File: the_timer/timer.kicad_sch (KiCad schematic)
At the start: 20 parts, among them J1 AVR-ISP-6, J2 Conn_01x04_Socket, J3 Conn_01x02_Socket, Q1 2N7002, Q2 2N7002, Q3 2N7002, U1 ATtiny48-A, U2 TPS61033, U3 MC3416, U4 W25Q128JVS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

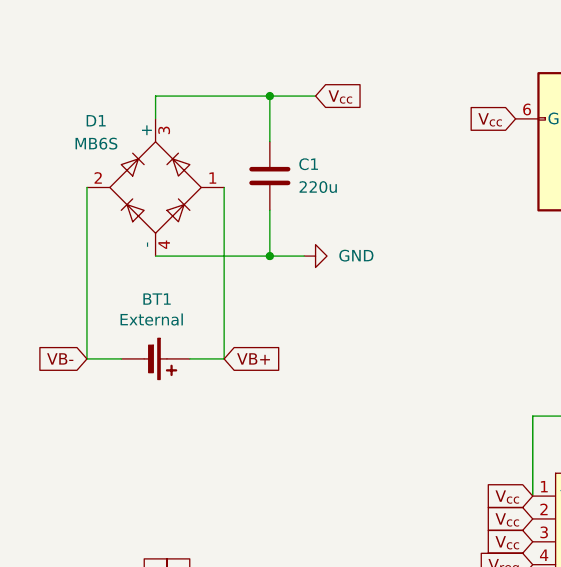
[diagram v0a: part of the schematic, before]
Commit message: repair timer files from the merge
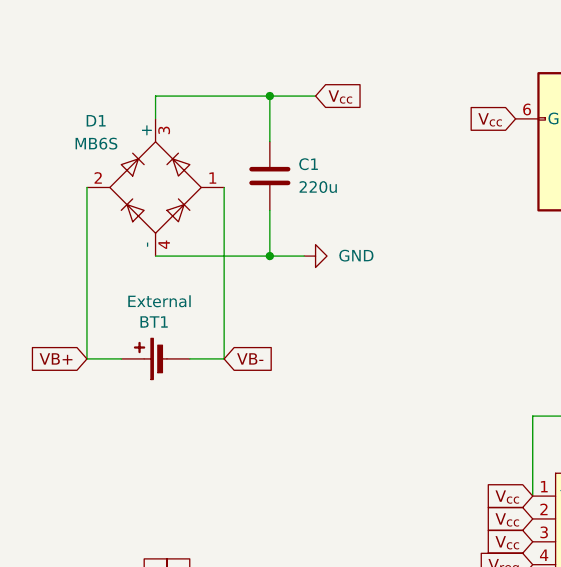
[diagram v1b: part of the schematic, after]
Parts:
- BT1: footprint locals:CONN2_1775469-2_TEC -> locals:TE Right Angle JST
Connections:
- net VB+: now also D1.2; no longer D1.1
- net VB-: now also D1.1; no longer D1.2
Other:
- moved on the sheet: BT1

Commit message: weekends'
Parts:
- C1: DKPN (none) -> STOCK
- D1: DKPN (none) -> MB6SCT-ND
- H1, H2, H3, J1, J2, J3: DKPN (none) -> CONN
- U4: DKPN (none) -> W25Q128JVSIQ-ND
- U5: DKPN (none) -> 223-1198-1-ND
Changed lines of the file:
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@@
+			)
+		)
+		(property "DKPN" "CONN"
+			(at 85.725 33.02 0)
+			(effects
+				(font
+					(size 1.27 1.27)
+				)
+				(hide yes)
 			)
 		)
@@
 			)
 		)
+		(property "DKPN" "CONN"
+			(at 184.15 92.71 0)
+			(effects
+				(font
+					(size 1.27 1.27)
+				)
+				(hide yes)
+			)
+		)
 		(pin "1"
 		)
@@
 			)
 		)
+		(property "DKPN" "CONN"
+			(at 109.22 149.86 0)
+			(effects
+				(font
+					(size 1.27 1.27)
+				)
+				(hide yes)
+			)
+		)
 		(instances
 			(project "timer"
@@
 			)
 		)
+		(property "DKPN" "CONN"
+			(at 185.42 111.76 0)
+			(effects
+				(font
+					(size 1.27 1.27)
+				)
+				(hide yes)
+			)
+		)
 		(pin "1"
 		)
@@
 			)
 		)
-		(property "DKPN" ""
+		(property "DKPN" "STOCK"
 			(at 48.26 36.83 0)
 			(effects
@@
 			)
 		)
+		(property "DKPN" "W25Q128JVSIQ-ND"
+			(at 87.63 113.03 0)
+			(effects
+				(font
+					(size 1.27 1.27)
+				)
+				(hide yes)
+			)
+		)
 		(pin "6"
 		)
@@
 		)
 		(property "Description" "Miniature Glass Passivated Single-Phase Surface Mount Bridge Rectifiers, 700V Vrms, 1.0A If, DFS SMD package"
+			(at 35.56 38.1 0)
+			(effects
+				(font
+					(size 1.27 1.27)
+				)
+				(hide yes)
+			)
+		)
+		(property "DKPN" "MB6SCT-ND"
 			(at 35.56 38.1 0)
 			(effects
@@
 			)
 		)
+		(property "DKPN" "CONN"
+			(at 82.55 149.86 0)
+			(effects
+				(font
+					(size 1.27 1.27)
+				)
+				(hide yes)
+			)
+		)
 		(instances
 			(project "timer"
@@
 			)
 		)
+		(property "DKPN" "CONN"
+			(at 137.16 149.86 0)
+			(effects
+				(font
+					(size 1.27 1.27)
+				)
+				(hide yes)
+			)
+		)
 		(instances
 			(project "timer"
@@
 			(at 139.7 110.49 0)
 			(effects
+				(font
+					(size 1.27 1.27)
+				)
+				(hide yes)
+			)
+		)
+		(property "DKPN" "223-1198-1-ND"
+			(at 139.7 110.49 0)
+			(effects

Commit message: Added decoupling cap to barometer and rotated IMU 45 deg
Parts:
- added C2: 100n, Capacitor_SMD:C_0603_1608Metric, symbol Device:C_Small
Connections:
- net GND: now also C2.2
- net V_{reg}: now also C2.1
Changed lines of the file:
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@@
 	)
 	(junction
+		(at 139.7 120.65)
+		(diameter 0)
+		(color 0 0 0 0)
+	)
+	(junction
 		(at 107.95 72.39)
 		(diameter 0)
@@
 	(wire
 		(pts
+			(xy 153.67 120.65) (xy 153.67 113.03)
+		)
+		(stroke
+			(width 0)
+			(type default)
+		)
+	)
+	(wire
+		(pts
 			(xy 85.09 63.5) (xy 77.47 63.5)
 		)
@@
 	(wire
 		(pts
+			(xy 139.7 100.33) (xy 153.67 100.33)
+		)
+		(stroke
+			(width 0)
+			(type default)
+		)
+	)
+	(wire
+		(pts
 			(xy 39.37 57.15) (xy 43.18 57.15)
 		)
@@
 	(wire
 		(pts
+			(xy 153.67 100.33) (xy 153.67 107.95)
+		)
+		(stroke
+			(width 0)
+			(type default)
+		)
+	)
+	(wire
+		(pts
 			(xy 90.17 63.5) (xy 99.06 63.5)
 		)
@@
 	(wire
 		(pts
+			(xy 139.7 120.65) (xy 153.67 120.65)
+		)
+		(stroke
+			(width 0)
+			(type default)
+		)
+	)
+	(wire
+		(pts
 			(xy 31.75 57.15) (xy 27.94 57.15)
 		)
@@
 	)
 	(symbol
+		(lib_id "Device:C_Small")
+		(at 153.67 110.49 0)
+		(unit 1)
+		(exclude_from_sim no)
+		(in_bom yes)
+		(on_board yes)
+		(dnp no)
+		(fields_autoplaced yes)
+		(property "Reference" "C2"
+			(at 156.21 109.2262 0)
+			(effects
+				(font
+					(size 1.27 1.27)
+				)
+				(justify left)
+			)
+		)
+		(property "Value" "100n"
+			(at 156.21 111.7662 0)
+			(effects
+				(font
+					(size 1.27 1.27)
+				)
+				(justify left)
+			)
+		)
+		(property "Footprint" "Capacitor_SMD:C_0603_1608Metric"
+			(at 153.67 110.49 0)
+			(effects
+				(font
+					(size 1.27 1.27)
+				)
+				(hide yes)
+			)
+		)
+		(property "Datasheet" "~"
+			(at 153.67 110.49 0)
+			(effects
+				(font
+					(size 1.27 1.27)
+				)
+				(hide yes)
+			)
+		)
+		(property "Description" "Unpolarized capacitor, small symbol"
+			(at 153.67 110.49 0)
+			(effects
+				(font
+					(size 1.27 1.27)
+				)
+				(hide yes)
+			)
+		)
+		(pin "2"
+		)
+		(pin "1"
+		)
+		(instances
+			(project "timer"
+				(path "/e2b0a296-fcac-4dcc-93f1-26b3dc1147d1"
+					(reference "C2")
+					(unit 1)
+				)
+			)
+		)
+	)
+	(symbol
 		(lib_id "globals:MC3416")
 		(at 135.255 34.925 0)
@@
 		(on_board yes)
 		(dnp no)
-		(fields_autoplaced yes)
 		(property "Reference" "#PWR013"
 			(at 123.19 115.57 0)
@@
 		)
 		(property "Value" "GND"
-			(at 125.73 115.5699 90)
+			(at 129.794 118.11 90)
 			(effects
 				(font
@@
 		(on_board yes)
 		(dnp no)
-		(fields_autoplaced yes)
 		(property "Reference" "U5"
-			(at 148.59 109.2199 0)
+			(at 121.666 95.25 0)
 			(effects
 				(font
@@
 		)
 		(property "Value" "MS5607-02BA"
-			(at 148.59 111.7599 0)
+			(at 121.666 97.79 0)
 			(effects
 				(font

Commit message: Updated barometer decoupling cap DKPN
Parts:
- C2: DKPN (none) -> 3372-0603B104J500XDTR-ND
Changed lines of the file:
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@@
 		(title "Timer")
 		(date "2024-04-16")
-		(rev "0.0.2")
+		(rev "0.0.3")
 		(company "Mines Rocket Club")
 		(comment 1 "William Layne")
@@
 			(at 153.67 110.49 0)
 			(effects
+				(font
+					(size 1.27 1.27)
+				)
+				(hide yes)
+			)
+		)
+		(property "DKPN" "3372-0603B104J500XDTR-ND"
+			(at 153.67 110.49 0)
+			(effects

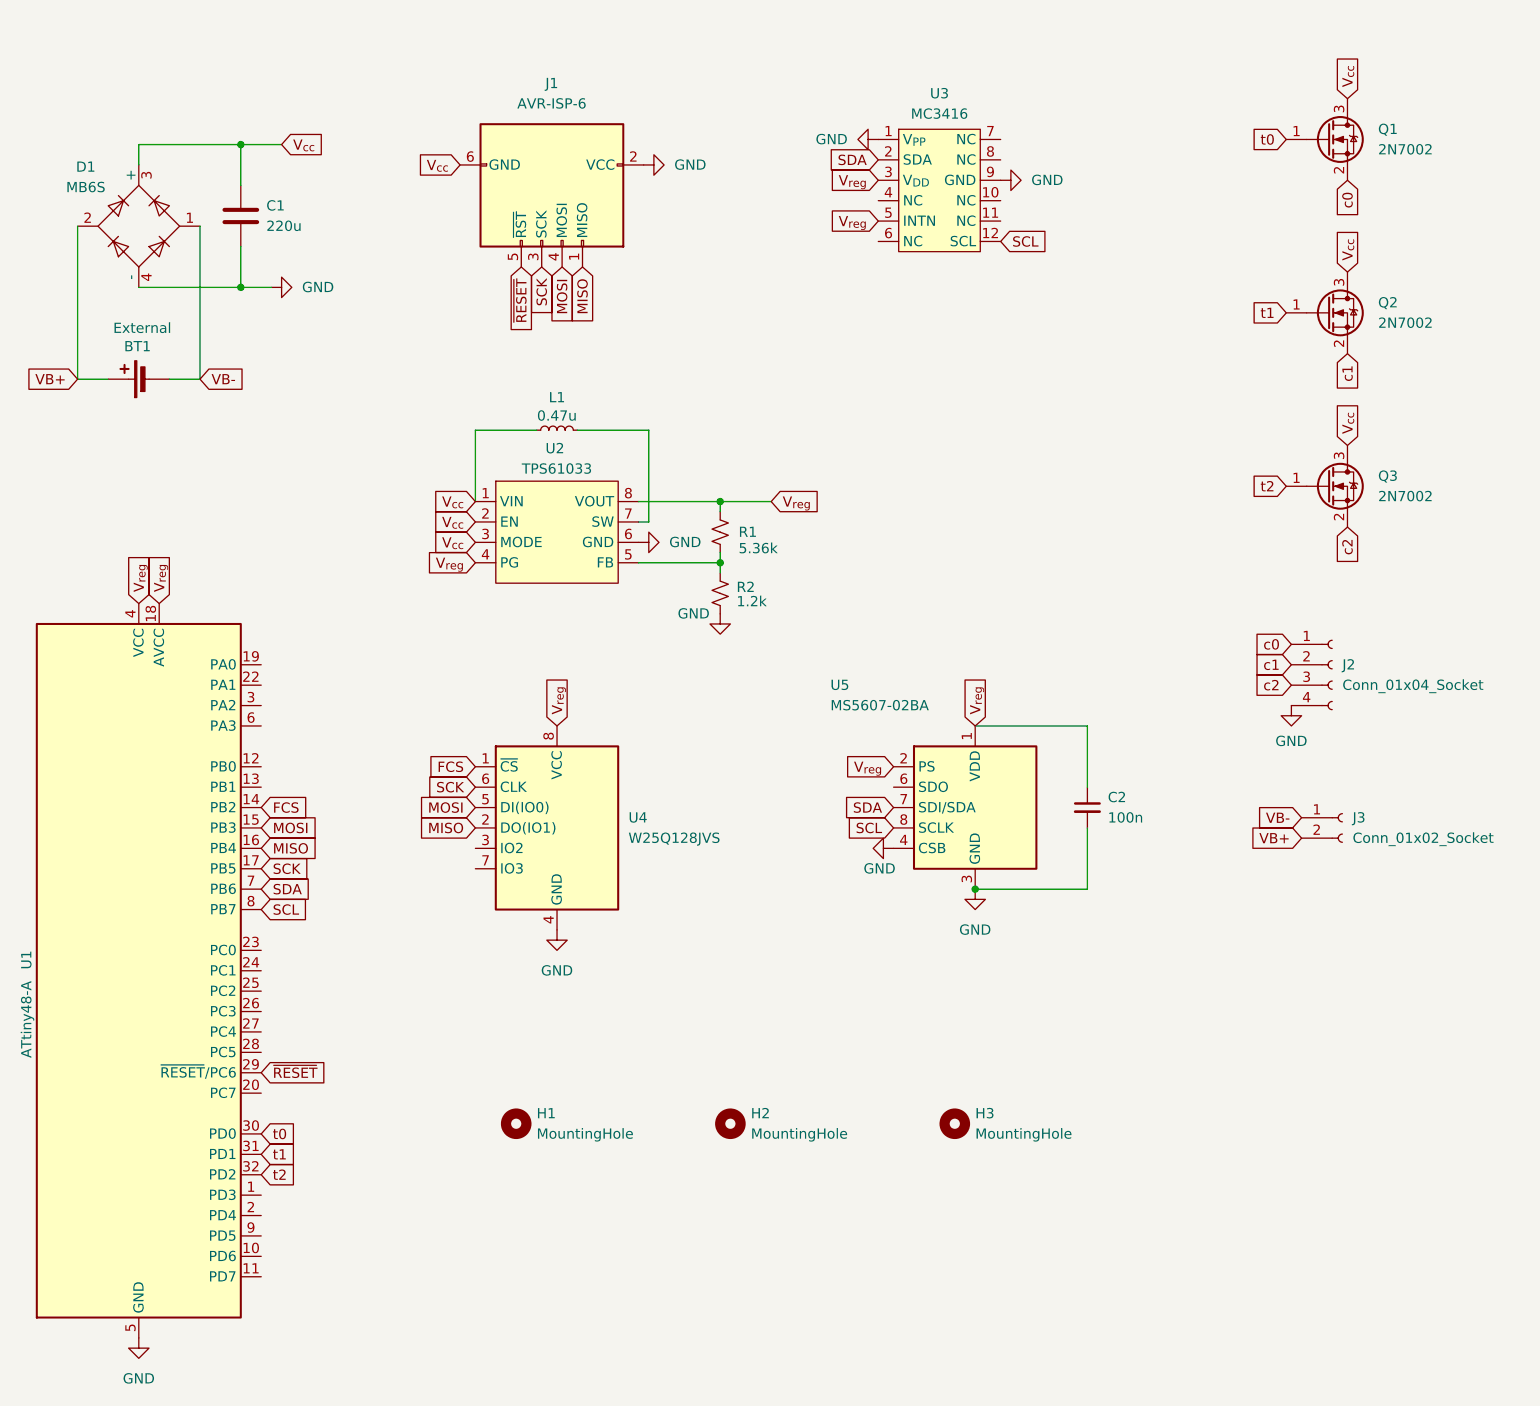
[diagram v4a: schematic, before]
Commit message: Standardized names on Timer schematic
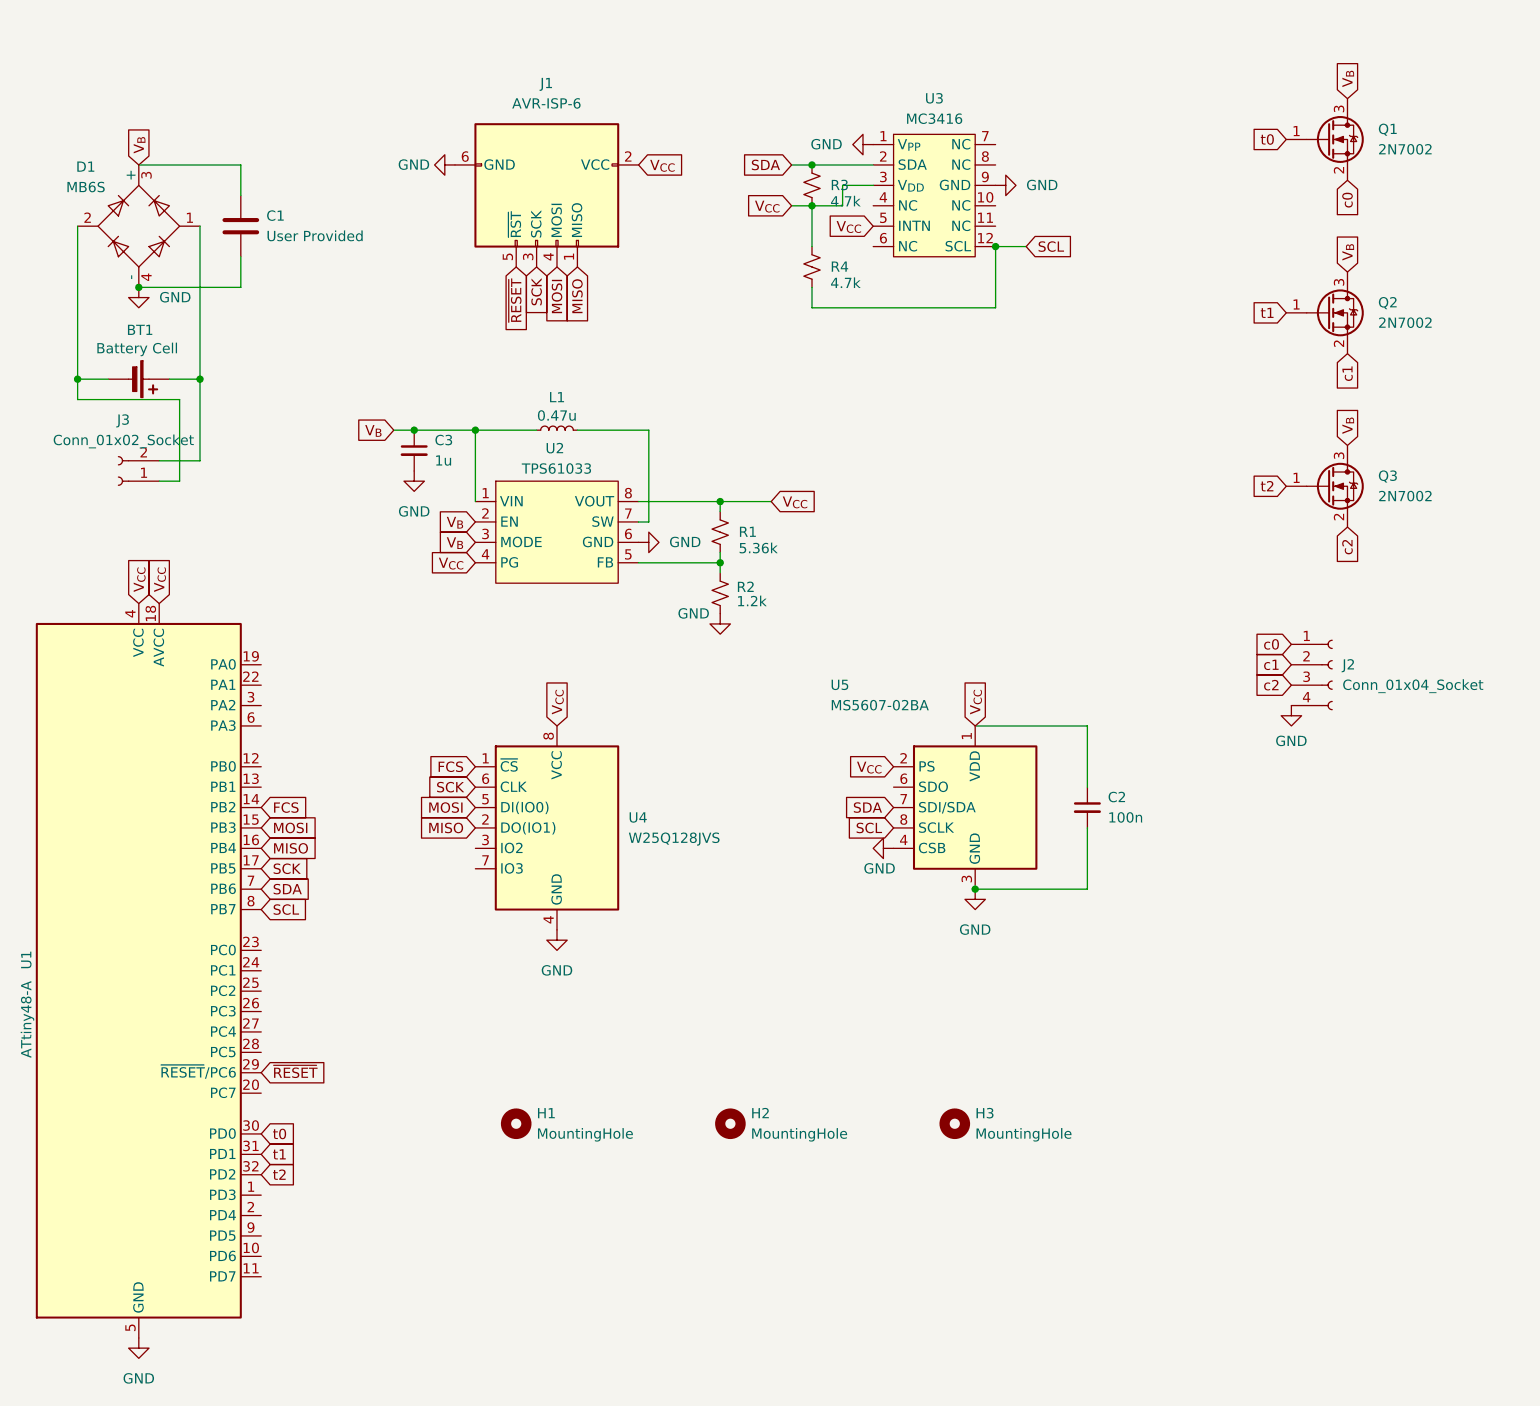
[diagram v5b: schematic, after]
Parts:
- added C3: 1u, Capacitor_SMD:C_0603_1608Metric, symbol Device:C_Small
- added R3, R4: 4.7k, Resistor_SMD:R_0603_1608Metric, symbol Device:R_Small_US
- BT1: value External -> Battery Cell; footprint locals:TE Right Angle JST -> locals_but_working_PLEASE:CONN2_1775469-2_TEC
- C1: value 220u -> User Provided; footprint Capacitor_THT:CP_Radial_D5.0mm_P2.00mm -> Connector_Wire:SolderWire-0.5sqmm_1x02_P4.8mm_D0.9mm_OD2.3mm; DKPN STOCK -> (none)
- C2: DKPN 3372-0603B104J500XDTR-ND -> 732-7989-1-ND
- L1: DKPN 490-LQM18DN470M70LCT-ND -> 732-7447860247CT-ND
- R1: DKPN RN73H1JTTD5361F10 -> RMCF0603FT5K36CT-ND
- R2: DKPN RN73R1JTTD1201F10 -> RMCF0603FT1K20CT-ND
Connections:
- net GND: now also J1.6 (GND), C3.2; no longer J1.2 (VCC)
- net SCL: now also R4.2
- net SDA: now also R3.1
- net VB+: no longer names the net of BT1.1 (+), J3.2 (Pin_2)
- net VB+: now also D1.1; no longer D1.2
- net VB-: no longer names the net of BT1.2 (-), J3.1 (Pin_1)
- net VB-: now also D1.2; no longer D1.1
- net V_{cc} renamed V_{B}
- net V_{B}: now also C3.1; no longer J1.6 (GND)
- net V_{reg} renamed V_{CC}
- net V_{CC}: now also J1.2 (VCC), R3.2, R4.1
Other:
- moved on the sheet: BT1, C1, J1, J3, U3

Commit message: gathered data on pyro charges
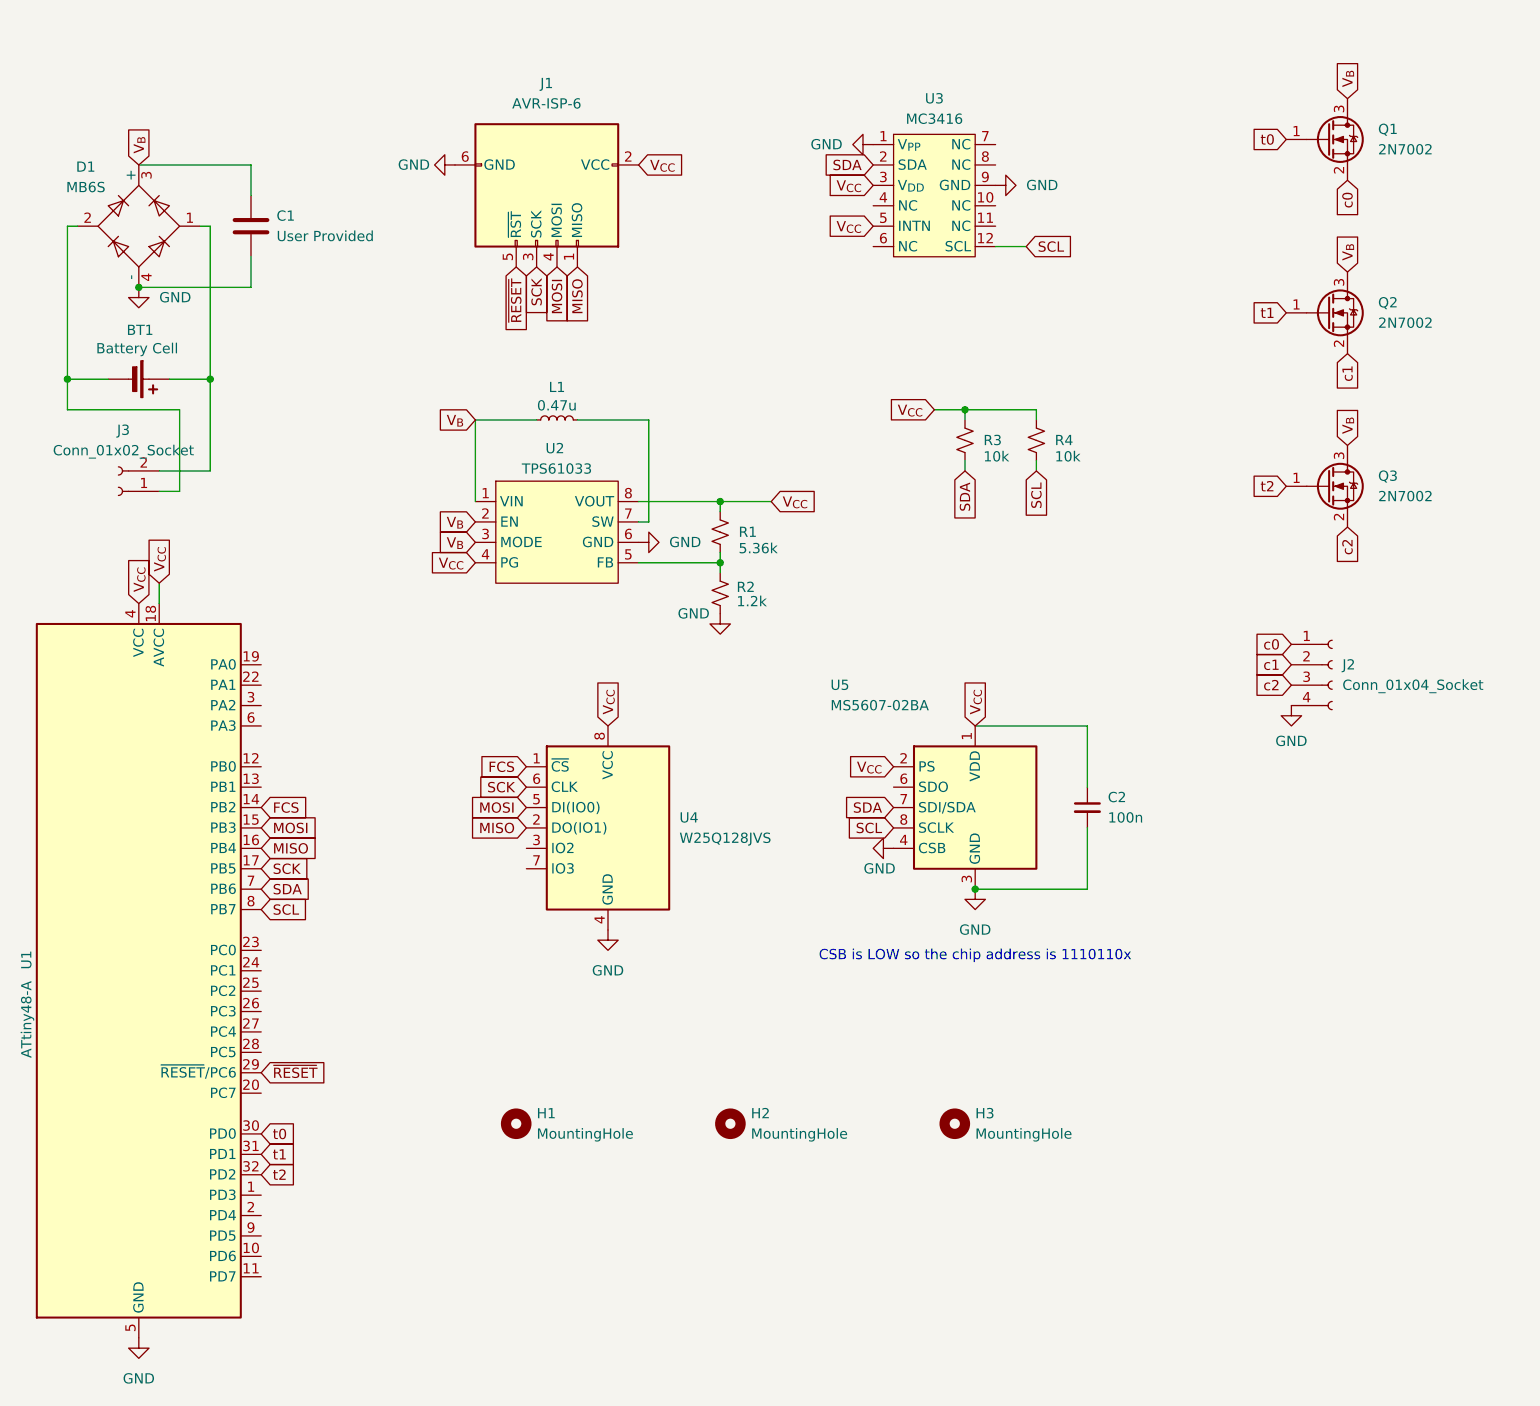
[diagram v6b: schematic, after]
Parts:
- removed C3: 1u, Capacitor_SMD:C_0603_1608Metric, symbol Device:C_Small
- R3, R4: value 4.7k -> 10k; DKPN RMCF0603FT4K70CT-ND -> RMCF0603JT10K0CT-ND
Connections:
- net SDA: now also R3.2; no longer R3.1
- net V_{CC}: now also R3.1; no longer R3.2
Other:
- note added: "CSB is LOW so the chip address is 1110110x"
- moved on the sheet: C1, J3, L1, U4
